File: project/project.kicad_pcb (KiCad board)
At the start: 2 copper layers, 85.5 x 86 mm, 260 parts, among them J1 FFC Connector, J2 input_1x5, J3 input_1x5, J4 input_1x5, J5 input_1x5, J6 input_1x5, J7 input_1x5, J8 input_1x5, J9 input_1x5, Q1 MMBTA44, Q10 MMBTA44, Q11 MMBTA44, Q12 MMBTA44, Q13 MMBTA44, Q14 MMBTA44, Q15 MMBTA44, Q16 MMBTA44, Q2 MMBTA44, Q3 MMBTA44, Q4 MMBTA44, Q5 MMBTA44, Q6 MMBTA44, Q7 MMBTA44, Q8 MMBTA44, Q9 MMBTA44, U1 PCA9555PW, U10 LTV-244-GB-G, U2 74HC165, U3 ISO1540, U4 GX101, U5 74HC165, U6 LTV-244-GB-G, U7 LTV-244-GB-G, U8 LTV-244-GB-G, U9 L78L05

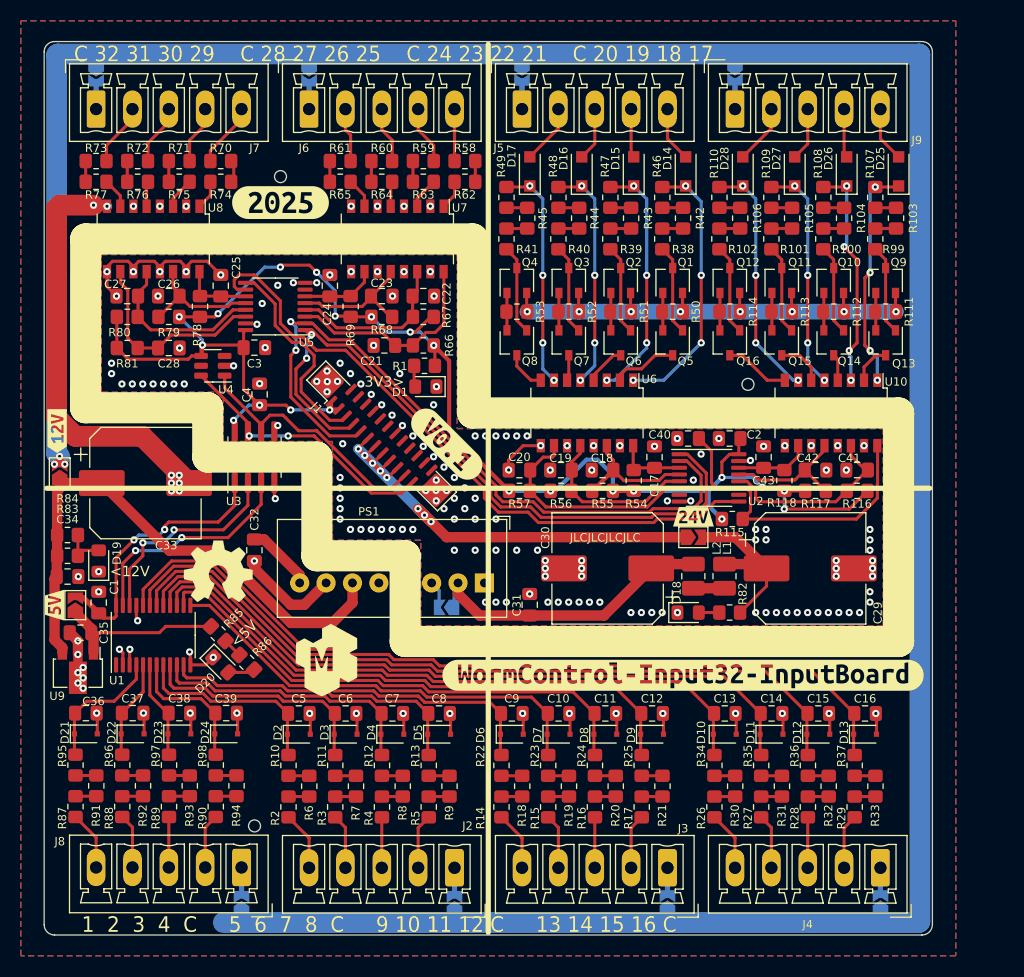
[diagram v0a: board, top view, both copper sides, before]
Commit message: refactoring everything to use selected input type
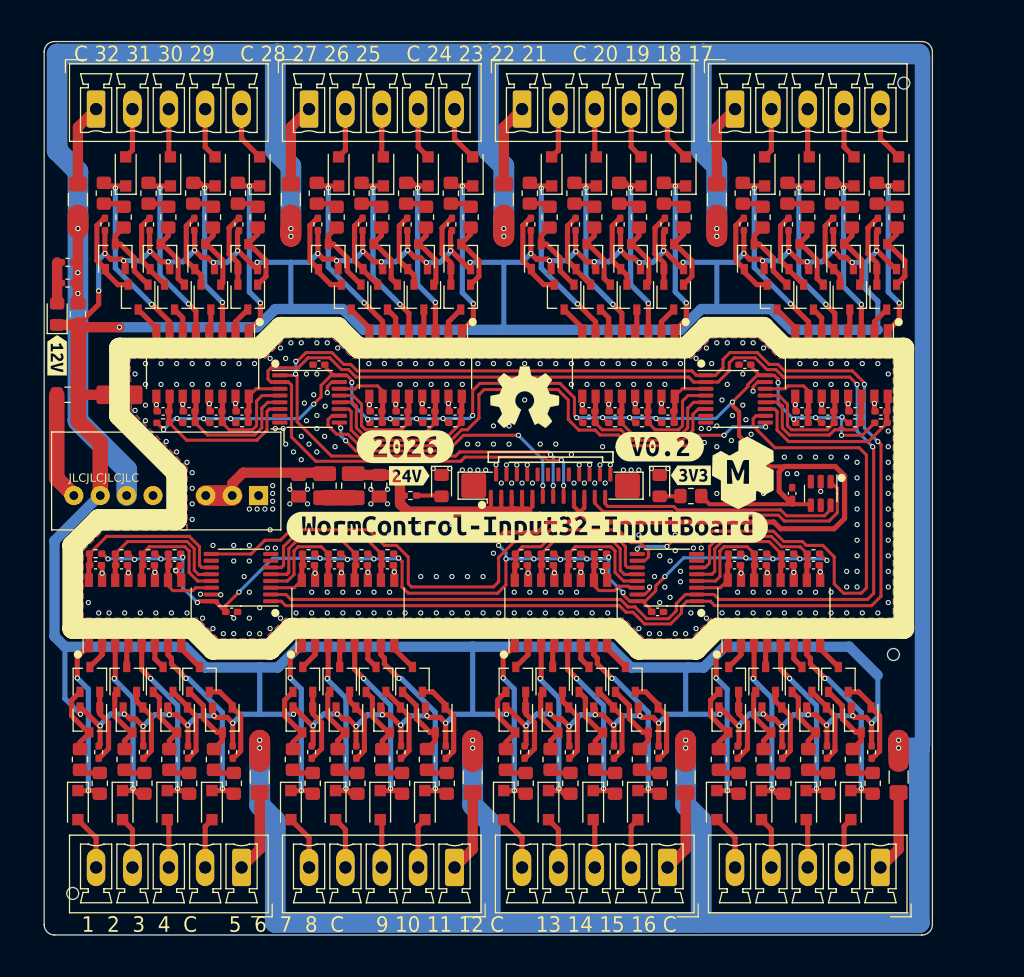
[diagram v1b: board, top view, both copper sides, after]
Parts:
- removed C1, C18, C19, C20, C21, C22, C23, C24, C25, C26, C27, C28, C34, C35, C41, C42, C43: 100n, Capacitor_SMD:C_0805_2012Metric_Pad1.18x1.45mm_HandSolder
- removed C10, C11, C12, C13, C14, C15, C16, C36, C37, C38, C39, C5, C6, C7, C8, C9: 10n, Capacitor_SMD:C_0805_2012Metric_Pad1.18x1.45mm_HandSolder
- removed C29, C30, C33: 220u/35v, Capacitor_SMD:CP_Elec_10x10.5
- removed D10, D11, D12, D13, D2, D21, D22, D23, D24, D3, D4, D5, D6, D7, D8, D9: UDZVTE-175.1B, Diode_SMD:D_SOD-323F
- removed D15, D16, D17, D26, D27, D28: SM4007PL, Diode_SMD:D_SOD-123F
- removed D20: GREEN, LED_SMD:LED_0805_2012Metric_Pad1.15x1.40mm_HandSolder
- removed J2, J3, J4, J6, J7, J8: input_1x5, Connector_Phoenix_MC:PhoenixContact_MCV_1,5_5-G-3.5_1x05_P3.50mm_Vertical
- removed JP1, JP10, JP11, JP12, JP2, JP3, JP4, JP5, JP6, JP7, JP8, JP9: SolderJumper_2_Open, Jumper:SolderJumper-2_P1.3mm_Open_TrianglePad1.0x1.5mm
- removed Q10, Q11, Q12, Q14, Q15, Q16, Q2, Q3, Q4, Q6, Q7, Q8: MMBTA44, Package_TO_SOT_SMD:SOT-23W
- removed R10, R100, R102, R104, R105, R106, R108, R109, R11, R110, R12, R13, R14, R15, R16, R17, R18, R19, R2, R20, R21, R22, R23, R24, R25, R26, R27, R28, R29, R3, R30, R31, R32, R33, R34, R35, R36, R37, R38, R39, R4, R40, R41, R43, R44, R45, R47, R48, R49, R5, R6, R7, R8, R87, R88, R89, R9, R90, R91, R92, R93, R94, R95, R96, R97, R98, R99: 150k, Resistor_SMD:R_0805_2012Metric_Pad1.20x1.40mm_HandSolder
- removed the R101 at (195.5, 67.0)
- removed R112, R113, R114, R51, R52, R53: 330R, Resistor_SMD:R_0805_2012Metric_Pad1.20x1.40mm_HandSolder
- removed R116, R117, R118, R55, R56, R57, R66, R67, R68, R69, R78, R79, R80, R81: 47k, Resistor_SMD:R_0805_2012Metric_Pad1.20x1.40mm_HandSolder
- removed R58, R59, R60, R61, R62, R63, R64, R65, R70, R71, R72, R73, R74, R75, R76, R77: 1k2, Resistor_SMD:R_0805_2012Metric_Pad1.20x1.40mm_HandSolder
- removed R85, R86: 4k7, Resistor_SMD:R_0805_2012Metric_Pad1.20x1.40mm_HandSolder
- removed U1: PCA9555PW, Package_SO:TSSOP-24_4.4x7.8mm_P0.65mm
- removed U10, U6, U7, U8: LTV-244-GB-G, Package_SO:SOP-16_4.4x10.4mm_P1.27mm
- removed U3: ISO1540, Package_SO:SOIC-8_3.9x4.9mm_P1.27mm
- removed U9: L78L05, Package_TO_SOT_SMD:SOT-89-3
- removed kibuzzard-68463028: G***, kibuzzard-68463028
- removed kibuzzard-68463097: G***, kibuzzard-68463097
- removed kibuzzard-68463581: G***, kibuzzard-68463581
- removed kibuzzard-68463930: G***, kibuzzard-68463930
- removed kibuzzard-68463AFF: G***, kibuzzard-68463AFF
- removed kibuzzard-68463C37 (x8): G***, kibuzzard-68463C37
- removed kibuzzard-68464180: G***, kibuzzard-68464180
- added C1002: 100n, Capacitor_SMD:C_0402_1005Metric_Pad0.74x0.62mm_HandSolder, F.Cu at (133.0, 98.4)
- added C1003: 100n, Capacitor_SMD:C_0402_1005Metric_Pad0.74x0.62mm_HandSolder, F.Cu at (135.6, 98.4)
- added C1004: 100n, Capacitor_SMD:C_0402_1005Metric_Pad0.74x0.62mm_HandSolder, F.Cu at (138.1, 98.4)
- added C102: 100n, Capacitor_SMD:C_0402_1005Metric_Pad0.74x0.62mm_HandSolder, F.Cu at (193.0, 79.1)
- added C105: 100n, Capacitor_SMD:C_0402_1005Metric_Pad0.74x0.62mm_HandSolder, F.Cu at (152.0, 79.1)
- added C201: 100n, Capacitor_SMD:C_0402_1005Metric_Pad0.74x0.62mm_HandSolder, F.Cu at (171.5, 98.4)
- added C202: 100n, Capacitor_SMD:C_0402_1005Metric_Pad0.74x0.62mm_HandSolder, F.Cu at (174.0, 98.4)
- added C203: 100n, Capacitor_SMD:C_0402_1005Metric_Pad0.74x0.62mm_HandSolder, F.Cu at (176.6, 98.4)
- added C204: 100n, Capacitor_SMD:C_0402_1005Metric_Pad0.74x0.62mm_HandSolder, F.Cu at (179.1, 98.4)
- added C301: 100n, Capacitor_SMD:C_0402_1005Metric_Pad0.74x0.62mm_HandSolder, F.Cu at (192.0, 98.4)
- added C302: 100n, Capacitor_SMD:C_0402_1005Metric_Pad0.74x0.62mm_HandSolder, F.Cu at (194.5, 98.4)
- added C303: 100n, Capacitor_SMD:C_0402_1005Metric_Pad0.74x0.62mm_HandSolder, F.Cu at (197.1, 98.4)
- added C304: 100n, Capacitor_SMD:C_0402_1005Metric_Pad0.74x0.62mm_HandSolder, F.Cu at (199.6, 98.4)
- added C401: 100n, Capacitor_SMD:C_0402_1005Metric_Pad0.74x0.62mm_HandSolder, F.Cu at (185.6, 83.6)
- added C402: 100n, Capacitor_SMD:C_0402_1005Metric_Pad0.74x0.62mm_HandSolder, F.Cu at (183.1, 83.6)
- added C403: 100n, Capacitor_SMD:C_0402_1005Metric_Pad0.74x0.62mm_HandSolder, F.Cu at (180.5, 83.6)
- added C404: 100n, Capacitor_SMD:C_0402_1005Metric_Pad0.74x0.62mm_HandSolder, F.Cu at (178.0, 83.6)
- added C502: 100n, Capacitor_SMD:C_0402_1005Metric_Pad0.74x0.62mm_HandSolder, F.Cu at (153.5, 98.4)
- added C503: 100n, Capacitor_SMD:C_0402_1005Metric_Pad0.74x0.62mm_HandSolder, F.Cu at (156.1, 98.4)
- added C504: 100n, Capacitor_SMD:C_0402_1005Metric_Pad0.74x0.62mm_HandSolder, F.Cu at (158.6, 98.4)
- added C601: 100n, Capacitor_SMD:C_0402_1005Metric_Pad0.74x0.62mm_HandSolder, F.Cu at (206.1, 83.6)
- added C602: 100n, Capacitor_SMD:C_0402_1005Metric_Pad0.74x0.62mm_HandSolder, F.Cu at (203.6, 83.6)
- added C603: 100n, Capacitor_SMD:C_0402_1005Metric_Pad0.74x0.62mm_HandSolder, F.Cu at (201.0, 83.6)
- added C604: 100n, Capacitor_SMD:C_0402_1005Metric_Pad0.74x0.62mm_HandSolder, F.Cu at (198.5, 83.6)
- added C701: 100n, Capacitor_SMD:C_0402_1005Metric_Pad0.74x0.62mm_HandSolder, F.Cu at (165.1, 83.6)
- added C702: 100n, Capacitor_SMD:C_0402_1005Metric_Pad0.74x0.62mm_HandSolder, F.Cu at (162.6, 83.6)
- added C703: 100n, Capacitor_SMD:C_0402_1005Metric_Pad0.74x0.62mm_HandSolder, F.Cu at (160.0, 83.6)
- added C704: 100n, Capacitor_SMD:C_0402_1005Metric_Pad0.74x0.62mm_HandSolder, F.Cu at (157.5, 83.6)
- added C801: 100n, Capacitor_SMD:C_0402_1005Metric_Pad0.74x0.62mm_HandSolder, F.Cu at (144.6, 83.6)
- added C802: 100n, Capacitor_SMD:C_0402_1005Metric_Pad0.74x0.62mm_HandSolder, F.Cu at (142.1, 83.6)
- added C803: 100n, Capacitor_SMD:C_0402_1005Metric_Pad0.74x0.62mm_HandSolder, F.Cu at (139.5, 83.6)
- added C804: 100n, Capacitor_SMD:C_0402_1005Metric_Pad0.74x0.62mm_HandSolder, F.Cu at (137.0, 83.6)
- added C901: 10u/50v, Capacitor_SMD:C_0805_2012Metric_Pad1.18x1.45mm_HandSolder, F.Cu at (157.8, 90.8)
- added C903: 1n/2KV, Capacitor_SMD:C_1206_3216Metric_Pad1.33x1.80mm_HandSolder, F.Cu at (132.8, 82.0)
- added C905: 22u/25v, Capacitor_SMD:C_0805_2012Metric_Pad1.18x1.45mm_HandSolder, F.Cu at (128.8, 74.3)
- added D1002: SM4007PL, Diode_SMD:D_SOD-123F, F.Cu at (133.1, 121.5)
- added D1003: SM4007PL, Diode_SMD:D_SOD-123F, F.Cu at (137.4, 121.5)
- added D1004: SM4007PL, Diode_SMD:D_SOD-123F, F.Cu at (141.7, 121.5)
- added D201: SM4007PL, Diode_SMD:D_SOD-123F, F.Cu at (169.8, 121.5)
- added D202: SM4007PL, Diode_SMD:D_SOD-123F, F.Cu at (174.1, 121.5)
- added D203: SM4007PL, Diode_SMD:D_SOD-123F, F.Cu at (178.4, 121.5)
- added D204: SM4007PL, Diode_SMD:D_SOD-123F, F.Cu at (182.7, 121.5)
- added D301: SM4007PL, Diode_SMD:D_SOD-123F, F.Cu at (190.3, 121.5)
- added D302: SM4007PL, Diode_SMD:D_SOD-123F, F.Cu at (194.6, 121.5)
- added D303: SM4007PL, Diode_SMD:D_SOD-123F, F.Cu at (198.9, 121.5)
- added D304: SM4007PL, Diode_SMD:D_SOD-123F, F.Cu at (203.2, 121.5)
- added D401: SM4007PL, Diode_SMD:D_SOD-123F, F.Cu at (187.3, 60.5)
- added D402: SM4007PL, Diode_SMD:D_SOD-123F, F.Cu at (183.0, 60.5)
- added D403: SM4007PL, Diode_SMD:D_SOD-123F, F.Cu at (178.7, 60.5)
- added D404: SM4007PL, Diode_SMD:D_SOD-123F, F.Cu at (174.4, 60.5)
- added D502: SM4007PL, Diode_SMD:D_SOD-123F, F.Cu at (153.6, 121.5)
- added D503: SM4007PL, Diode_SMD:D_SOD-123F, F.Cu at (157.9, 121.5)
- added D504: SM4007PL, Diode_SMD:D_SOD-123F, F.Cu at (162.2, 121.5)
- added D601: SM4007PL, Diode_SMD:D_SOD-123F, F.Cu at (207.8, 60.5)
- added D602: SM4007PL, Diode_SMD:D_SOD-123F, F.Cu at (203.5, 60.5)
- added D603: SM4007PL, Diode_SMD:D_SOD-123F, F.Cu at (199.2, 60.5)
- added D604: SM4007PL, Diode_SMD:D_SOD-123F, F.Cu at (194.9, 60.5)
- added D701: SM4007PL, Diode_SMD:D_SOD-123F, F.Cu at (166.8, 60.5)
- added D702: SM4007PL, Diode_SMD:D_SOD-123F, F.Cu at (162.5, 60.5)
- added D703: SM4007PL, Diode_SMD:D_SOD-123F, F.Cu at (158.2, 60.5)
- added D704: SM4007PL, Diode_SMD:D_SOD-123F, F.Cu at (153.9, 60.5)
- added D801: SM4007PL, Diode_SMD:D_SOD-123F, F.Cu at (146.3, 60.5)
- added D802: SM4007PL, Diode_SMD:D_SOD-123F, F.Cu at (142.0, 60.5)
- added D803: SM4007PL, Diode_SMD:D_SOD-123F, F.Cu at (137.7, 60.5)
- added D804: SM4007PL, Diode_SMD:D_SOD-123F, F.Cu at (133.4, 60.5)
- added F1001: 50mA, Fuse:Fuse_1206_3216Metric_Pad1.42x1.75mm_HandSolder, F.Cu at (146.3, 118.8)
- added F201: 50mA, Fuse:Fuse_1206_3216Metric_Pad1.42x1.75mm_HandSolder, F.Cu at (187.3, 118.8)
- added F301: 50mA, Fuse:Fuse_1206_3216Metric_Pad1.42x1.75mm_HandSolder, F.Cu at (207.8, 118.8)
- added F401: 50mA, Fuse:Fuse_1206_3216Metric_Pad1.42x1.75mm_HandSolder, F.Cu at (169.8, 63.2)
- added F501: 50mA, Fuse:Fuse_1206_3216Metric_Pad1.42x1.75mm_HandSolder, F.Cu at (166.8, 118.8)
- added F601: 50mA, Fuse:Fuse_1206_3216Metric_Pad1.42x1.75mm_HandSolder, F.Cu at (190.3, 63.2)
- added F701: 50mA, Fuse:Fuse_1206_3216Metric_Pad1.42x1.75mm_HandSolder, F.Cu at (149.3, 63.2)
- added F801: 50mA, Fuse:Fuse_1206_3216Metric_Pad1.42x1.75mm_HandSolder, F.Cu at (128.8, 63.2)
- added J201: input_1x5, Connector_Phoenix_MC:PhoenixContact_MCV_1,5_5-G-3.5_1x05_P3.50mm_Vertical, F.Cu at (185.5, 127.5)
- added J301: input_1x5, Connector_Phoenix_MC:PhoenixContact_MCV_1,5_5-G-3.5_1x05_P3.50mm_Vertical, F.Cu at (206.0, 127.5)
- added J401: input_1x5, Connector_Phoenix_MC:PhoenixContact_MCV_1,5_5-G-3.5_1x05_P3.50mm_Vertical, F.Cu at (171.5, 54.5)
- added J601: input_1x5, Connector_Phoenix_MC:PhoenixContact_MCV_1,5_5-G-3.5_1x05_P3.50mm_Vertical, F.Cu at (192.0, 54.5)
- added J701: input_1x5, Connector_Phoenix_MC:PhoenixContact_MCV_1,5_5-G-3.5_1x05_P3.50mm_Vertical, F.Cu at (151.0, 54.5)
- added J801: input_1x5, Connector_Phoenix_MC:PhoenixContact_MCV_1,5_5-G-3.5_1x05_P3.50mm_Vertical, F.Cu at (130.5, 54.5)
- added Q1002: MMBTA44, Package_TO_SOT_SMD:SOT-23W, F.Cu at (134.1, 113.3)
- added Q1003: MMBTA44, Package_TO_SOT_SMD:SOT-23W, F.Cu at (138.4, 113.3)
- added Q1004: MMBTA44, Package_TO_SOT_SMD:SOT-23W, F.Cu at (142.7, 113.3)
- added Q1006: MMBTA44, Package_TO_SOT_SMD:SOT-23W, F.Cu at (133.5, 109.4)
- added Q1007: MMBTA44, Package_TO_SOT_SMD:SOT-23W, F.Cu at (137.0, 109.4)
- added Q1008: MMBTA44, Package_TO_SOT_SMD:SOT-23W, F.Cu at (140.5, 109.4)
- added Q201: MMBTA44, Package_TO_SOT_SMD:SOT-23W, F.Cu at (170.9, 113.3)
- added Q202: MMBTA44, Package_TO_SOT_SMD:SOT-23W, F.Cu at (175.1, 113.3)
- added Q203: MMBTA44, Package_TO_SOT_SMD:SOT-23W, F.Cu at (179.4, 113.3)
- added Q204: MMBTA44, Package_TO_SOT_SMD:SOT-23W, F.Cu at (183.7, 113.3)
- added Q205: MMBTA44, Package_TO_SOT_SMD:SOT-23W, F.Cu at (170.9, 109.4)
- added Q206: MMBTA44, Package_TO_SOT_SMD:SOT-23W, F.Cu at (174.5, 109.4)
- added Q207: MMBTA44, Package_TO_SOT_SMD:SOT-23W, F.Cu at (178.0, 109.4)
- added Q208: MMBTA44, Package_TO_SOT_SMD:SOT-23W, F.Cu at (181.5, 109.4)
- added Q301: MMBTA44, Package_TO_SOT_SMD:SOT-23W, F.Cu at (191.4, 113.3)
- added Q302: MMBTA44, Package_TO_SOT_SMD:SOT-23W, F.Cu at (195.6, 113.3)
- added Q303: MMBTA44, Package_TO_SOT_SMD:SOT-23W, F.Cu at (199.9, 113.3)
- added Q304: MMBTA44, Package_TO_SOT_SMD:SOT-23W, F.Cu at (204.2, 113.3)
- added Q305: MMBTA44, Package_TO_SOT_SMD:SOT-23W, F.Cu at (191.4, 109.4)
- added Q306: MMBTA44, Package_TO_SOT_SMD:SOT-23W, F.Cu at (195.0, 109.4)
- added Q307: MMBTA44, Package_TO_SOT_SMD:SOT-23W, F.Cu at (198.5, 109.4)
- added Q308: MMBTA44, Package_TO_SOT_SMD:SOT-23W, F.Cu at (202.0, 109.4)
- added Q401: MMBTA44, Package_TO_SOT_SMD:SOT-23W, F.Cu at (186.1, 68.7)
- added Q402: MMBTA44, Package_TO_SOT_SMD:SOT-23W, F.Cu at (182.0, 68.7)
- added Q403: MMBTA44, Package_TO_SOT_SMD:SOT-23W, F.Cu at (177.7, 68.7)
- added Q404: MMBTA44, Package_TO_SOT_SMD:SOT-23W, F.Cu at (173.4, 68.7)
- added Q405: MMBTA44, Package_TO_SOT_SMD:SOT-23W, F.Cu at (186.1, 72.6)
- added Q406: MMBTA44, Package_TO_SOT_SMD:SOT-23W, F.Cu at (182.6, 72.6)
- added Q407: MMBTA44, Package_TO_SOT_SMD:SOT-23W, F.Cu at (179.1, 72.6)
- added Q408: MMBTA44, Package_TO_SOT_SMD:SOT-23W, F.Cu at (175.6, 72.6)
- added Q502: MMBTA44, Package_TO_SOT_SMD:SOT-23W, F.Cu at (154.6, 113.3)
- added Q503: MMBTA44, Package_TO_SOT_SMD:SOT-23W, F.Cu at (158.9, 113.3)
- added Q504: MMBTA44, Package_TO_SOT_SMD:SOT-23W, F.Cu at (163.2, 113.3)
- added Q506: MMBTA44, Package_TO_SOT_SMD:SOT-23W, F.Cu at (154.0, 109.4)
- added Q507: MMBTA44, Package_TO_SOT_SMD:SOT-23W, F.Cu at (157.5, 109.4)
- added Q508: MMBTA44, Package_TO_SOT_SMD:SOT-23W, F.Cu at (161.0, 109.4)
- added Q601: MMBTA44, Package_TO_SOT_SMD:SOT-23W, F.Cu at (206.6, 68.7)
- added Q602: MMBTA44, Package_TO_SOT_SMD:SOT-23W, F.Cu at (202.5, 68.7)
- added Q603: MMBTA44, Package_TO_SOT_SMD:SOT-23W, F.Cu at (198.2, 68.7)
- added Q604: MMBTA44, Package_TO_SOT_SMD:SOT-23W, F.Cu at (193.9, 68.7)
- added Q605: MMBTA44, Package_TO_SOT_SMD:SOT-23W, F.Cu at (206.6, 72.6)
- added Q606: MMBTA44, Package_TO_SOT_SMD:SOT-23W, F.Cu at (203.1, 72.6)
- added Q607: MMBTA44, Package_TO_SOT_SMD:SOT-23W, F.Cu at (199.6, 72.6)
- added Q608: MMBTA44, Package_TO_SOT_SMD:SOT-23W, F.Cu at (196.1, 72.6)
- added Q701: MMBTA44, Package_TO_SOT_SMD:SOT-23W, F.Cu at (165.6, 68.7)
- added Q702: MMBTA44, Package_TO_SOT_SMD:SOT-23W, F.Cu at (161.5, 68.7)
- added Q703: MMBTA44, Package_TO_SOT_SMD:SOT-23W, F.Cu at (157.2, 68.7)
- added Q704: MMBTA44, Package_TO_SOT_SMD:SOT-23W, F.Cu at (152.9, 68.7)
- added Q705: MMBTA44, Package_TO_SOT_SMD:SOT-23W, F.Cu at (165.6, 72.6)
- added Q706: MMBTA44, Package_TO_SOT_SMD:SOT-23W, F.Cu at (162.1, 72.6)
- added Q707: MMBTA44, Package_TO_SOT_SMD:SOT-23W, F.Cu at (158.6, 72.6)
- added Q708: MMBTA44, Package_TO_SOT_SMD:SOT-23W, F.Cu at (155.1, 72.6)
- added Q801: MMBTA44, Package_TO_SOT_SMD:SOT-23W, F.Cu at (145.1, 68.7)
- added Q802: MMBTA44, Package_TO_SOT_SMD:SOT-23W, F.Cu at (141.0, 68.7)
- added Q803: MMBTA44, Package_TO_SOT_SMD:SOT-23W, F.Cu at (136.7, 68.7)
- added Q804: MMBTA44, Package_TO_SOT_SMD:SOT-23W, F.Cu at (132.4, 68.7)
- added Q805: MMBTA44, Package_TO_SOT_SMD:SOT-23W, F.Cu at (145.1, 72.6)
- added Q806: MMBTA44, Package_TO_SOT_SMD:SOT-23W, F.Cu at (141.6, 72.6)
- added Q807: MMBTA44, Package_TO_SOT_SMD:SOT-23W, F.Cu at (138.1, 72.6)
- added Q808: MMBTA44, Package_TO_SOT_SMD:SOT-23W, F.Cu at (134.6, 72.6)
- added R1002: 220k, Resistor_SMD:R_0805_2012Metric_Pad1.20x1.40mm_HandSolder, F.Cu at (133.3, 117.1)
- added R1003: 220k, Resistor_SMD:R_0805_2012Metric_Pad1.20x1.40mm_HandSolder, F.Cu at (137.6, 117.1)
- added R1004: 220k, Resistor_SMD:R_0805_2012Metric_Pad1.20x1.40mm_HandSolder, F.Cu at (141.9, 117.1)
- added R1006: 220k, Resistor_SMD:R_0805_2012Metric_Pad1.20x1.40mm_HandSolder, F.Cu at (135.2, 119.4)
- added R1007: 220k, Resistor_SMD:R_0805_2012Metric_Pad1.20x1.40mm_HandSolder, F.Cu at (139.5, 119.4)
- added R1008: 220k, Resistor_SMD:R_0805_2012Metric_Pad1.20x1.40mm_HandSolder, F.Cu at (143.8, 119.4)
- added R1010: 330R, Resistor_SMD:R_0402_1005Metric_Pad0.72x0.64mm_HandSolder, F.Cu at (135.1, 116.4)
- added R1011: 330R, Resistor_SMD:R_0402_1005Metric_Pad0.72x0.64mm_HandSolder, F.Cu at (139.4, 116.4)
- added R1012: 330R, Resistor_SMD:R_0402_1005Metric_Pad0.72x0.64mm_HandSolder, F.Cu at (143.7, 116.4)
- added R1014: 47k, Resistor_SMD:R_0402_1005Metric_Pad0.72x0.64mm_HandSolder, F.Cu at (133.0, 97.3)
- added R1015: 47k, Resistor_SMD:R_0402_1005Metric_Pad0.72x0.64mm_HandSolder, F.Cu at (135.6, 97.3)
- added R1016: 47k, Resistor_SMD:R_0402_1005Metric_Pad0.72x0.64mm_HandSolder, F.Cu at (138.1, 97.3)
- added R201: 220k, Resistor_SMD:R_0805_2012Metric_Pad1.20x1.40mm_HandSolder, F.Cu at (170.0, 117.1)
- added R202: 220k, Resistor_SMD:R_0805_2012Metric_Pad1.20x1.40mm_HandSolder, F.Cu at (174.3, 117.1)
- added R203: 220k, Resistor_SMD:R_0805_2012Metric_Pad1.20x1.40mm_HandSolder, F.Cu at (178.6, 117.1)
- added R204: 220k, Resistor_SMD:R_0805_2012Metric_Pad1.20x1.40mm_HandSolder, F.Cu at (182.9, 117.1)
- added R205: 220k, Resistor_SMD:R_0805_2012Metric_Pad1.20x1.40mm_HandSolder, F.Cu at (171.9, 119.4)
- added R206: 220k, Resistor_SMD:R_0805_2012Metric_Pad1.20x1.40mm_HandSolder, F.Cu at (176.2, 119.4)
- added R207: 220k, Resistor_SMD:R_0805_2012Metric_Pad1.20x1.40mm_HandSolder, F.Cu at (180.5, 119.4)
- added R208: 220k, Resistor_SMD:R_0805_2012Metric_Pad1.20x1.40mm_HandSolder, F.Cu at (184.8, 119.4)
- added R209: 330R, Resistor_SMD:R_0402_1005Metric_Pad0.72x0.64mm_HandSolder, F.Cu at (171.8, 116.4)
- added R210: 330R, Resistor_SMD:R_0402_1005Metric_Pad0.72x0.64mm_HandSolder, F.Cu at (176.1, 116.4)
- added R211: 330R, Resistor_SMD:R_0402_1005Metric_Pad0.72x0.64mm_HandSolder, F.Cu at (180.4, 116.4)
- added R212: 330R, Resistor_SMD:R_0402_1005Metric_Pad0.72x0.64mm_HandSolder, F.Cu at (184.7, 116.4)
- added R213: 47k, Resistor_SMD:R_0402_1005Metric_Pad0.72x0.64mm_HandSolder, F.Cu at (171.5, 97.3)
- added R214: 47k, Resistor_SMD:R_0402_1005Metric_Pad0.72x0.64mm_HandSolder, F.Cu at (174.0, 97.3)
- added R215: 47k, Resistor_SMD:R_0402_1005Metric_Pad0.72x0.64mm_HandSolder, F.Cu at (176.6, 97.3)
- added R216: 47k, Resistor_SMD:R_0402_1005Metric_Pad0.72x0.64mm_HandSolder, F.Cu at (179.1, 97.3)
- added R301: 220k, Resistor_SMD:R_0805_2012Metric_Pad1.20x1.40mm_HandSolder, F.Cu at (190.5, 117.1)
- added R302: 220k, Resistor_SMD:R_0805_2012Metric_Pad1.20x1.40mm_HandSolder, F.Cu at (194.8, 117.1)
- added R303: 220k, Resistor_SMD:R_0805_2012Metric_Pad1.20x1.40mm_HandSolder, F.Cu at (199.1, 117.1)
- added R304: 220k, Resistor_SMD:R_0805_2012Metric_Pad1.20x1.40mm_HandSolder, F.Cu at (203.4, 117.1)
- added R305: 220k, Resistor_SMD:R_0805_2012Metric_Pad1.20x1.40mm_HandSolder, F.Cu at (192.4, 119.4)
- added R306: 220k, Resistor_SMD:R_0805_2012Metric_Pad1.20x1.40mm_HandSolder, F.Cu at (196.7, 119.4)
- added R307: 220k, Resistor_SMD:R_0805_2012Metric_Pad1.20x1.40mm_HandSolder, F.Cu at (201.0, 119.4)
- added R308: 220k, Resistor_SMD:R_0805_2012Metric_Pad1.20x1.40mm_HandSolder, F.Cu at (205.3, 119.4)
- added R309: 330R, Resistor_SMD:R_0402_1005Metric_Pad0.72x0.64mm_HandSolder, F.Cu at (192.3, 116.4)
- added R310: 330R, Resistor_SMD:R_0402_1005Metric_Pad0.72x0.64mm_HandSolder, F.Cu at (196.6, 116.4)
- added R311: 330R, Resistor_SMD:R_0402_1005Metric_Pad0.72x0.64mm_HandSolder, F.Cu at (200.9, 116.4)
- added R312: 330R, Resistor_SMD:R_0402_1005Metric_Pad0.72x0.64mm_HandSolder, F.Cu at (205.2, 116.4)
- added R313: 47k, Resistor_SMD:R_0402_1005Metric_Pad0.72x0.64mm_HandSolder, F.Cu at (192.0, 97.3)
- added R314: 47k, Resistor_SMD:R_0402_1005Metric_Pad0.72x0.64mm_HandSolder, F.Cu at (194.5, 97.3)
- added R315: 47k, Resistor_SMD:R_0402_1005Metric_Pad0.72x0.64mm_HandSolder, F.Cu at (197.1, 97.3)
- added R316: 47k, Resistor_SMD:R_0402_1005Metric_Pad0.72x0.64mm_HandSolder, F.Cu at (199.6, 97.3)
- added R401: 220k, Resistor_SMD:R_0805_2012Metric_Pad1.20x1.40mm_HandSolder, F.Cu at (187.1, 64.9)
- added R402: 220k, Resistor_SMD:R_0805_2012Metric_Pad1.20x1.40mm_HandSolder, F.Cu at (182.8, 64.9)
- added R403: 220k, Resistor_SMD:R_0805_2012Metric_Pad1.20x1.40mm_HandSolder, F.Cu at (178.5, 64.9)
- added R404: 220k, Resistor_SMD:R_0805_2012Metric_Pad1.20x1.40mm_HandSolder, F.Cu at (174.2, 64.9)
- added R405: 220k, Resistor_SMD:R_0805_2012Metric_Pad1.20x1.40mm_HandSolder, F.Cu at (185.2, 62.6)
- added R406: 220k, Resistor_SMD:R_0805_2012Metric_Pad1.20x1.40mm_HandSolder, F.Cu at (180.9, 62.6)
- added R407: 220k, Resistor_SMD:R_0805_2012Metric_Pad1.20x1.40mm_HandSolder, F.Cu at (176.6, 62.6)
- added R408: 220k, Resistor_SMD:R_0805_2012Metric_Pad1.20x1.40mm_HandSolder, F.Cu at (172.3, 62.6)
- added R409: 330R, Resistor_SMD:R_0402_1005Metric_Pad0.72x0.64mm_HandSolder, F.Cu at (185.3, 65.6)
- added R410: 330R, Resistor_SMD:R_0402_1005Metric_Pad0.72x0.64mm_HandSolder, F.Cu at (181.0, 65.6)
- added R411: 330R, Resistor_SMD:R_0402_1005Metric_Pad0.72x0.64mm_HandSolder, F.Cu at (176.7, 65.6)
- added R412: 330R, Resistor_SMD:R_0402_1005Metric_Pad0.72x0.64mm_HandSolder, F.Cu at (172.4, 65.6)
- added R413: 47k, Resistor_SMD:R_0402_1005Metric_Pad0.72x0.64mm_HandSolder, F.Cu at (185.6, 84.7)
- added R414: 47k, Resistor_SMD:R_0402_1005Metric_Pad0.72x0.64mm_HandSolder, F.Cu at (183.1, 84.7)
- added R415: 47k, Resistor_SMD:R_0402_1005Metric_Pad0.72x0.64mm_HandSolder, F.Cu at (180.5, 84.7)
- added R416: 47k, Resistor_SMD:R_0402_1005Metric_Pad0.72x0.64mm_HandSolder, F.Cu at (178.0, 84.7)
- added R502: 220k, Resistor_SMD:R_0805_2012Metric_Pad1.20x1.40mm_HandSolder, F.Cu at (153.8, 117.1)
- added R503: 220k, Resistor_SMD:R_0805_2012Metric_Pad1.20x1.40mm_HandSolder, F.Cu at (158.1, 117.1)
- added R504: 220k, Resistor_SMD:R_0805_2012Metric_Pad1.20x1.40mm_HandSolder, F.Cu at (162.4, 117.1)
- added R506: 220k, Resistor_SMD:R_0805_2012Metric_Pad1.20x1.40mm_HandSolder, F.Cu at (155.7, 119.4)
- added R507: 220k, Resistor_SMD:R_0805_2012Metric_Pad1.20x1.40mm_HandSolder, F.Cu at (160.0, 119.4)
- added R508: 220k, Resistor_SMD:R_0805_2012Metric_Pad1.20x1.40mm_HandSolder, F.Cu at (164.3, 119.4)
- added R510: 330R, Resistor_SMD:R_0402_1005Metric_Pad0.72x0.64mm_HandSolder, F.Cu at (155.6, 116.4)
- added R511: 330R, Resistor_SMD:R_0402_1005Metric_Pad0.72x0.64mm_HandSolder, F.Cu at (159.9, 116.4)
- added R512: 330R, Resistor_SMD:R_0402_1005Metric_Pad0.72x0.64mm_HandSolder, F.Cu at (164.2, 116.4)
- added R514: 47k, Resistor_SMD:R_0402_1005Metric_Pad0.72x0.64mm_HandSolder, F.Cu at (153.5, 97.3)
- added R515: 47k, Resistor_SMD:R_0402_1005Metric_Pad0.72x0.64mm_HandSolder, F.Cu at (156.1, 97.3)
- added R516: 47k, Resistor_SMD:R_0402_1005Metric_Pad0.72x0.64mm_HandSolder, F.Cu at (158.6, 97.3)
- added R601: 220k, Resistor_SMD:R_0805_2012Metric_Pad1.20x1.40mm_HandSolder, F.Cu at (207.6, 64.9)
- added R602: 220k, Resistor_SMD:R_0805_2012Metric_Pad1.20x1.40mm_HandSolder, F.Cu at (203.3, 64.9)
- added R603: 220k, Resistor_SMD:R_0805_2012Metric_Pad1.20x1.40mm_HandSolder, F.Cu at (199.0, 64.9)
- added R604: 220k, Resistor_SMD:R_0805_2012Metric_Pad1.20x1.40mm_HandSolder, F.Cu at (194.7, 64.9)
- added R605: 220k, Resistor_SMD:R_0805_2012Metric_Pad1.20x1.40mm_HandSolder, F.Cu at (205.7, 62.6)
- added R606: 220k, Resistor_SMD:R_0805_2012Metric_Pad1.20x1.40mm_HandSolder, F.Cu at (201.4, 62.6)
- added R607: 220k, Resistor_SMD:R_0805_2012Metric_Pad1.20x1.40mm_HandSolder, F.Cu at (197.1, 62.6)
- added R608: 220k, Resistor_SMD:R_0805_2012Metric_Pad1.20x1.40mm_HandSolder, F.Cu at (192.8, 62.6)
- added R609: 330R, Resistor_SMD:R_0402_1005Metric_Pad0.72x0.64mm_HandSolder, F.Cu at (205.8, 65.6)
- added R610: 330R, Resistor_SMD:R_0402_1005Metric_Pad0.72x0.64mm_HandSolder, F.Cu at (201.5, 65.6)
- added R611: 330R, Resistor_SMD:R_0402_1005Metric_Pad0.72x0.64mm_HandSolder, F.Cu at (197.2, 65.6)
- added R612: 330R, Resistor_SMD:R_0402_1005Metric_Pad0.72x0.64mm_HandSolder, F.Cu at (192.9, 65.6)
- added R613: 47k, Resistor_SMD:R_0402_1005Metric_Pad0.72x0.64mm_HandSolder, F.Cu at (206.1, 84.7)
- added R614: 47k, Resistor_SMD:R_0402_1005Metric_Pad0.72x0.64mm_HandSolder, F.Cu at (203.6, 84.7)
- added R615: 47k, Resistor_SMD:R_0402_1005Metric_Pad0.72x0.64mm_HandSolder, F.Cu at (201.0, 84.7)
- added R616: 47k, Resistor_SMD:R_0402_1005Metric_Pad0.72x0.64mm_HandSolder, F.Cu at (198.5, 84.7)
- added R701: 220k, Resistor_SMD:R_0805_2012Metric_Pad1.20x1.40mm_HandSolder, F.Cu at (166.6, 64.9)
- added R702: 220k, Resistor_SMD:R_0805_2012Metric_Pad1.20x1.40mm_HandSolder, F.Cu at (162.3, 64.9)
- added R703: 220k, Resistor_SMD:R_0805_2012Metric_Pad1.20x1.40mm_HandSolder, F.Cu at (158.0, 64.9)
- added R704: 220k, Resistor_SMD:R_0805_2012Metric_Pad1.20x1.40mm_HandSolder, F.Cu at (153.7, 64.9)
- added R705: 220k, Resistor_SMD:R_0805_2012Metric_Pad1.20x1.40mm_HandSolder, F.Cu at (164.7, 62.6)
- added R706: 220k, Resistor_SMD:R_0805_2012Metric_Pad1.20x1.40mm_HandSolder, F.Cu at (160.4, 62.6)
- added R707: 220k, Resistor_SMD:R_0805_2012Metric_Pad1.20x1.40mm_HandSolder, F.Cu at (156.1, 62.6)
- added R708: 220k, Resistor_SMD:R_0805_2012Metric_Pad1.20x1.40mm_HandSolder, F.Cu at (151.8, 62.6)
- added R709: 330R, Resistor_SMD:R_0402_1005Metric_Pad0.72x0.64mm_HandSolder, F.Cu at (164.8, 65.6)
- added R710: 330R, Resistor_SMD:R_0402_1005Metric_Pad0.72x0.64mm_HandSolder, F.Cu at (160.5, 65.6)
- added R711: 330R, Resistor_SMD:R_0402_1005Metric_Pad0.72x0.64mm_HandSolder, F.Cu at (156.2, 65.6)
- added R712: 330R, Resistor_SMD:R_0402_1005Metric_Pad0.72x0.64mm_HandSolder, F.Cu at (151.9, 65.6)
- added R713: 47k, Resistor_SMD:R_0402_1005Metric_Pad0.72x0.64mm_HandSolder, F.Cu at (165.1, 84.7)
- added R714: 47k, Resistor_SMD:R_0402_1005Metric_Pad0.72x0.64mm_HandSolder, F.Cu at (162.6, 84.7)
- added R715: 47k, Resistor_SMD:R_0402_1005Metric_Pad0.72x0.64mm_HandSolder, F.Cu at (160.0, 84.7)
- added R716: 47k, Resistor_SMD:R_0402_1005Metric_Pad0.72x0.64mm_HandSolder, F.Cu at (157.5, 84.7)
- added R801: 220k, Resistor_SMD:R_0805_2012Metric_Pad1.20x1.40mm_HandSolder, F.Cu at (146.1, 64.9)
- added R802: 220k, Resistor_SMD:R_0805_2012Metric_Pad1.20x1.40mm_HandSolder, F.Cu at (141.8, 64.9)
- added R803: 220k, Resistor_SMD:R_0805_2012Metric_Pad1.20x1.40mm_HandSolder, F.Cu at (137.5, 64.9)
- added R804: 220k, Resistor_SMD:R_0805_2012Metric_Pad1.20x1.40mm_HandSolder, F.Cu at (133.2, 64.9)
- added R805: 220k, Resistor_SMD:R_0805_2012Metric_Pad1.20x1.40mm_HandSolder, F.Cu at (144.2, 62.6)
- added R806: 220k, Resistor_SMD:R_0805_2012Metric_Pad1.20x1.40mm_HandSolder, F.Cu at (139.9, 62.6)
- added R807: 220k, Resistor_SMD:R_0805_2012Metric_Pad1.20x1.40mm_HandSolder, F.Cu at (135.6, 62.6)
- added R808: 220k, Resistor_SMD:R_0805_2012Metric_Pad1.20x1.40mm_HandSolder, F.Cu at (131.3, 62.6)
- added R809: 330R, Resistor_SMD:R_0402_1005Metric_Pad0.72x0.64mm_HandSolder, F.Cu at (144.3, 65.6)
- added R810: 330R, Resistor_SMD:R_0402_1005Metric_Pad0.72x0.64mm_HandSolder, F.Cu at (140.0, 65.6)
- added R811: 330R, Resistor_SMD:R_0402_1005Metric_Pad0.72x0.64mm_HandSolder, F.Cu at (135.7, 65.6)
- added R812: 330R, Resistor_SMD:R_0402_1005Metric_Pad0.72x0.64mm_HandSolder, F.Cu at (131.4, 65.6)
- added R813: 47k, Resistor_SMD:R_0402_1005Metric_Pad0.72x0.64mm_HandSolder, F.Cu at (144.6, 84.7)
- added R814: 47k, Resistor_SMD:R_0402_1005Metric_Pad0.72x0.64mm_HandSolder, F.Cu at (142.1, 84.7)
- added R815: 47k, Resistor_SMD:R_0402_1005Metric_Pad0.72x0.64mm_HandSolder, F.Cu at (139.5, 84.7)
- added R816: 47k, Resistor_SMD:R_0402_1005Metric_Pad0.72x0.64mm_HandSolder, F.Cu at (137.0, 84.7)
- added U1001: LTV-244-GB-G, Package_SO:SOP-16_4.4x10.4mm_P1.27mm, F.Cu at (134.3, 103.0)
- added U102: 74HC165, Package_SO:TSSOP-16_4.4x5mm_P0.65mm, F.Cu at (192.1, 82.4)
- added U105: 74HC165, Package_SO:TSSOP-16_4.4x5mm_P0.65mm, F.Cu at (151.1, 82.4)
- added U201: LTV-244-GB-G, Package_SO:SOP-16_4.4x10.4mm_P1.27mm, F.Cu at (175.3, 103.0)
- added U301: LTV-244-GB-G, Package_SO:SOP-16_4.4x10.4mm_P1.27mm, F.Cu at (195.8, 103.0)
- added U401: LTV-244-GB-G, Package_SO:SOP-16_4.4x10.4mm_P1.27mm, F.Cu at (181.8, 79.0)
- added U501: LTV-244-GB-G, Package_SO:SOP-16_4.4x10.4mm_P1.27mm, F.Cu at (154.8, 103.0)
- added U601: LTV-244-GB-G, Package_SO:SOP-16_4.4x10.4mm_P1.27mm, F.Cu at (202.3, 79.0)
- added U701: LTV-244-GB-G, Package_SO:SOP-16_4.4x10.4mm_P1.27mm, F.Cu at (161.3, 79.0)
- added U801: LTV-244-GB-G, Package_SO:SOP-16_4.4x10.4mm_P1.27mm, F.Cu at (140.8, 79.0)
- added kibuzzard-69735EB9: G***, kibuzzard-69735EB9, F.Cu at (184.8, 87.0)
- added kibuzzard-69735EC0: G***, kibuzzard-69735EC0, F.Cu at (160.3, 87.0)
- added kibuzzard-69799C4A: G***, kibuzzard-69799C4A, F.Cu at (160.7, 89.8)
- added kibuzzard-69799C58: G***, kibuzzard-69799C58, F.Cu at (126.8, 78.2)
- added kibuzzard-69799C9D: G***, kibuzzard-69799C9D, F.Cu at (187.8, 89.8)
- C1001: renamed from C40; footprint Capacitor_SMD:C_0805_2012Metric_Pad1.18x1.45mm_HandSolder -> Capacitor_SMD:C_0402_1005Metric_Pad0.74x0.62mm_HandSolder
- C101: renamed from C2; footprint Capacitor_SMD:C_0805_2012Metric_Pad1.18x1.45mm_HandSolder -> Capacitor_SMD:C_0402_1005Metric_Pad0.74x0.62mm_HandSolder
- C103: renamed from C4; footprint Capacitor_SMD:C_0805_2012Metric_Pad1.18x1.45mm_HandSolder -> Capacitor_SMD:C_0402_1005Metric_Pad0.74x0.62mm_HandSolder
- C104: renamed from C3; footprint Capacitor_SMD:C_0805_2012Metric_Pad1.18x1.45mm_HandSolder -> Capacitor_SMD:C_0402_1005Metric_Pad0.74x0.62mm_HandSolder
- C501: renamed from C17; footprint Capacitor_SMD:C_0805_2012Metric_Pad1.18x1.45mm_HandSolder -> Capacitor_SMD:C_0402_1005Metric_Pad0.74x0.62mm_HandSolder
- R1001: renamed from R103; value 150k -> 220k
- R1005: renamed from R107; value 150k -> 220k
- R1009: renamed from R111; footprint Resistor_SMD:R_0805_2012Metric_Pad1.20x1.40mm_HandSolder -> Resistor_SMD:R_0402_1005Metric_Pad0.72x0.64mm_HandSolder
- R1013: renamed from R115; footprint Resistor_SMD:R_0805_2012Metric_Pad1.20x1.40mm_HandSolder -> Resistor_SMD:R_0402_1005Metric_Pad0.72x0.64mm_HandSolder
- R501: renamed from R42; value 150k -> 220k
- R505: renamed from R46; value 150k -> 220k
- R509: renamed from R50; footprint Resistor_SMD:R_0805_2012Metric_Pad1.20x1.40mm_HandSolder -> Resistor_SMD:R_0402_1005Metric_Pad0.72x0.64mm_HandSolder
- R513: renamed from R54; footprint Resistor_SMD:R_0805_2012Metric_Pad1.20x1.40mm_HandSolder -> Resistor_SMD:R_0402_1005Metric_Pad0.72x0.64mm_HandSolder
- R901: renamed from R82; footprint Resistor_SMD:R_0805_2012Metric_Pad1.20x1.40mm_HandSolder -> Resistor_SMD:R_0402_1005Metric_Pad0.72x0.64mm_HandSolder
- R902: renamed from R83; footprint Resistor_SMD:R_0805_2012Metric_Pad1.20x1.40mm_HandSolder -> Resistor_SMD:R_0402_1005Metric_Pad0.72x0.64mm_HandSolder
- R903: renamed from R84; footprint Resistor_SMD:R_0805_2012Metric_Pad1.20x1.40mm_HandSolder -> Resistor_SMD:R_0402_1005Metric_Pad0.72x0.64mm_HandSolder
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- renumbered C31 to C902, C32 to C904, D25 to D1001, D1 to D101, D14 to D501, D18 to D901, D19 to D902, G1 to G101, G2 to G102, J9 to J1001, J1 to J101, J5 to J501, L1 to L901, L2 to L902, PS1 to PS901, Q9 to Q1001, Q13 to Q1005, Q1 to Q501, Q5 to Q505, R1 to R101, U2 to U101, U4 to U103, U5 to U104
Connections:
- net /_ser_link_1 renamed /_ser_link_3
- net /input2-1/O1 renamed /input1/O1
- net /input2-2/O1 renamed /input2/O1
- net Net-(D14-Pad1) renamed /input2/OP11
- net Net-(D25-Pad1) renamed /input1/OP11
- net Net-(Q1-Pad1) renamed /input2/B12
- net Net-(Q9-Pad1) renamed /input1/B12
- C902 pad 1: Net-(C30-Pad1) -> Net-(C902-Pad1)
- J1001 pad 1: /input2-1/12V -> Net-(F1001-Pad1)
- J101 pad 1: +3V3 -> +24V
- J101 pad 11: +24V -> SER_DATA
- J101 pad 13: +24V -> SER_PL
- J101 pad 15: +24V -> SER_CLK
- J101 pad 17: +24V -> +3V3
- J101 pad 19: +24V -> +3V3
- J101 pad 3: +3V3 -> +24V
- J101 pad 5: SER_DATA -> +24V
- J101 pad 7: SER_PL -> +24V
- J101 pad 9: SER_CLK -> +24V
- J501 pad 1: /input2-2/12V -> Net-(F501-Pad1)
- L901 pad 1: /power/24V -> +24V
- L902 pad 2: Net-(C30-Pad1) -> Net-(C902-Pad1)
- PS901 pad 2: Net-(C30-Pad1) -> Net-(C902-Pad1)
- PS901 pad 3: Net-(JP12-Pad2) -> Net-(C902-Pad1)
- PS901 pad 6: /power/12V -> +12P
- Q1001 pad 3: Net-(Q9-Pad3) -> /input1/B11
- Q1005 pad 1: Net-(Q9-Pad3) -> /input1/B11
- Q1005 pad 3: Net-(Q13-Pad3) -> /input1/OP12
- Q501 pad 3: Net-(Q1-Pad3) -> /input2/B11
- Q505 pad 1: Net-(Q1-Pad3) -> /input2/B11
- Q505 pad 3: Net-(Q5-Pad3) -> /input2/OP12
- R1001 pad 2: Net-(R103-Pad2) -> /input1/B11
- R501 pad 2: Net-(R38-Pad1) -> /input2/B11
- R901 pad 2: /power/24V -> +24V
- R902 pad 1: /power/12V -> +12P
- R903 pad 1: /power/12V -> +12P
- U101 pad 12: /input2-1/O2 -> /input1/O2
- U101 pad 13: /input2-1/O3 -> /input1/O3
- U101 pad 14: /input2-1/O4 -> /input1/O4
- U101 pad 4: /input2-2/O2 -> /input2/O2
- U101 pad 5: /input2-2/O3 -> /input2/O3
- U101 pad 6: /input2-2/O4 -> /input2/O4
- U104 pad 11: /input3-1/O1 -> /input3/O1
- U104 pad 12: /input3-1/O2 -> /input3/O2
- U104 pad 13: /input3-1/O3 -> /input3/O3
- U104 pad 14: /input3-1/O4 -> /input3/O4
- U104 pad 3: /input3-2/O1 -> /input4/O1
- U104 pad 4: /input3-2/O2 -> /input4/O2
- U104 pad 5: /input3-2/O3 -> /input4/O3
- U104 pad 6: /input3-2/O4 -> /input4/O4
- U104 pad 9: SER_DATA -> /_ser_link_2
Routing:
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- removed copper zone on B.Cu, net GNDPWR
- removed copper zone on F.Cu, net GNDPWR
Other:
- board text removed: "3V3>"
- board text removed: "<12V"
- board text removed: "<5V"

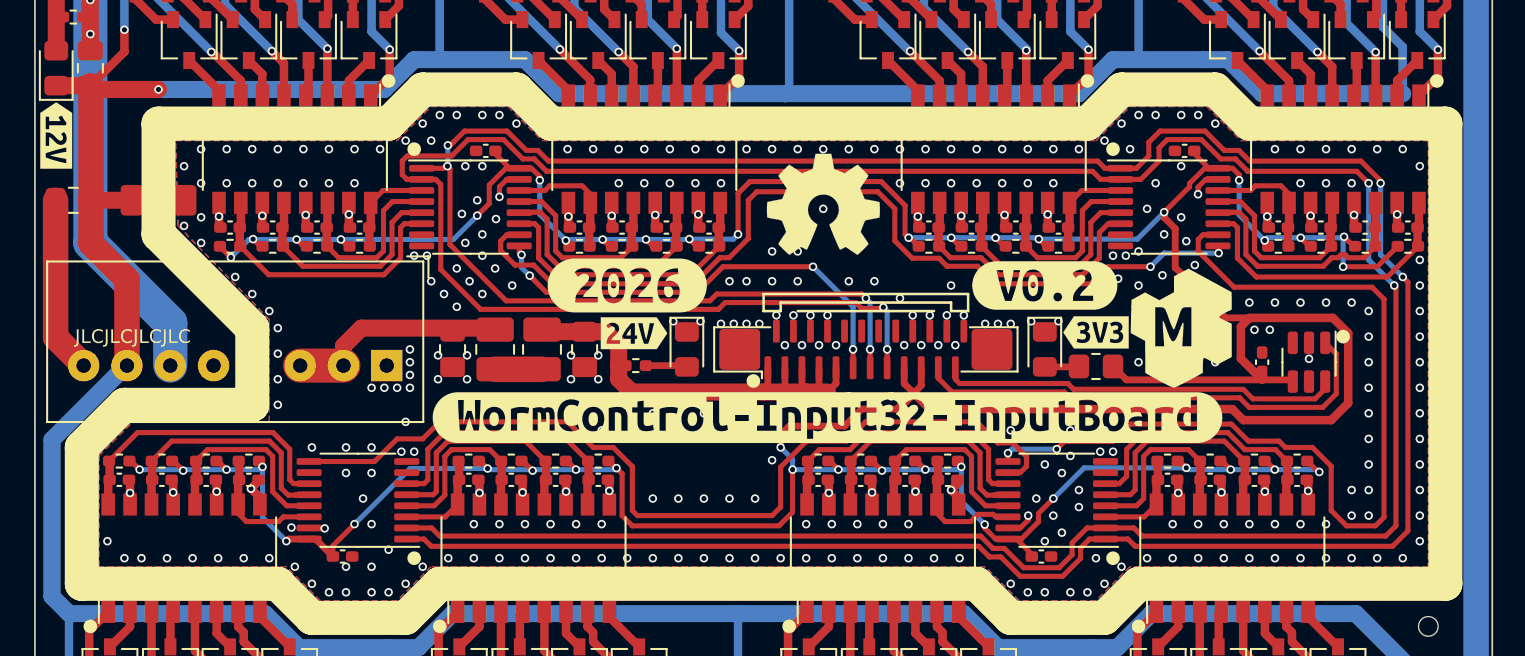
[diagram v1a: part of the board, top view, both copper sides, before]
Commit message: moving ffc connector to align with other boards
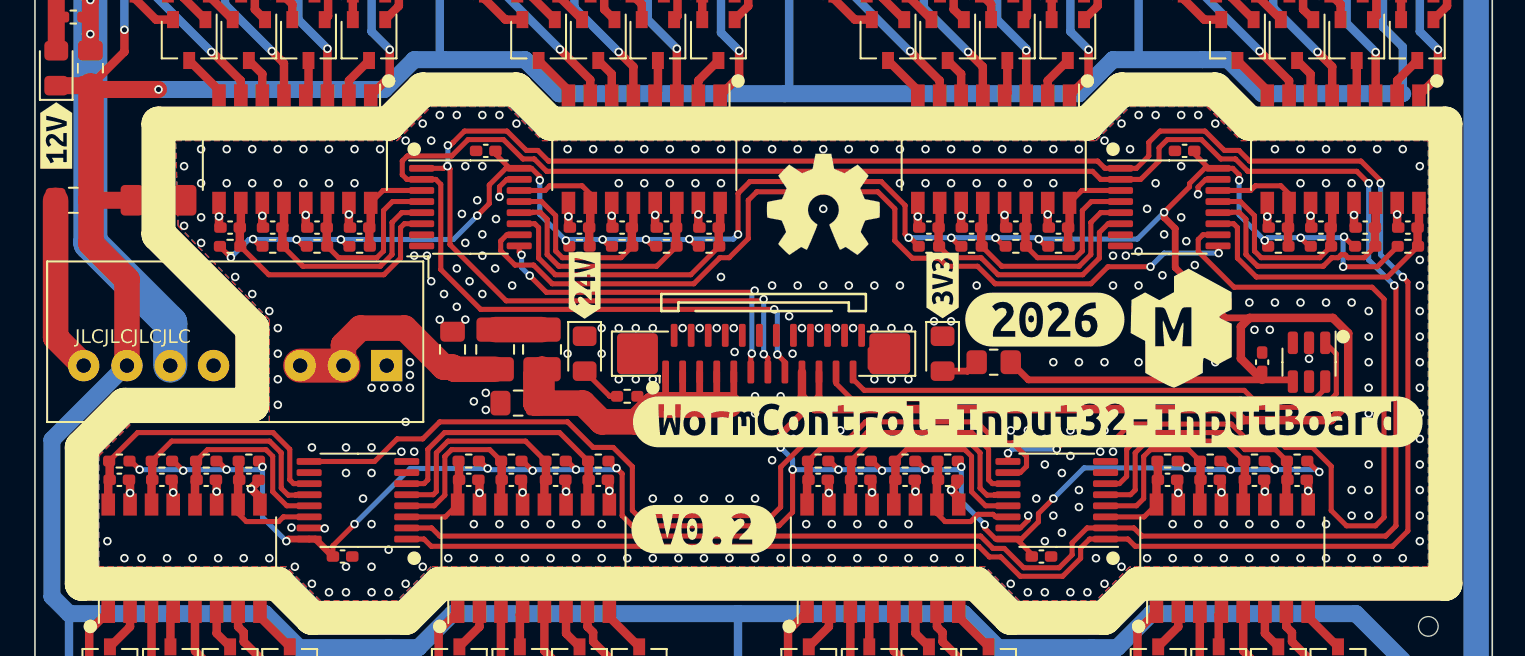
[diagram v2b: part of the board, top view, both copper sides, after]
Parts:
- removed kibuzzard-69799C4A: G***, kibuzzard-69799C4A
- removed kibuzzard-69799C58: G***, kibuzzard-69799C58
- added kibuzzard-698DC759: G***, kibuzzard-698DC759, F.Cu at (126.8, 78.2)
- added kibuzzard-698DC8DA: G***, kibuzzard-698DC8DA, F.Cu at (157.8, 87.0)
- moved kibuzzard-69735EB9 24.6 mm to (164.8, 101.3)
- moved kibuzzard-69735EC0 24.6 mm to (184.8, 89.0)
- moved kibuzzard-6846361F 11.8 mm to (183.8, 95.0)
- moved kibuzzard-69799C9D 9.41 mm to (178.8, 87.0), turned to 90 degrees
- moved D101 6.01 mm to (178.8, 91.0)
- moved D901 6.01 mm to (157.8, 91.0)
- moved J101 6.01 mm to (168.3, 91.0)
- moved R101 6.01 mm to (181.8, 91.5)
- moved C901 5.01 mm to (153.9, 93.9), turned to 180 degrees
- moved R901 1.87 mm to (160.3, 93.5), turned to 0 degrees
- turned C902 to 90 degrees
- turned L901 to 90 degrees
- turned L902 to -90 degrees
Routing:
- net SER_CLK: track 181.5 -> 175.0 mm
- net +3V3: track 278.1 -> 284.5 mm
- net SER_DATA: track 26.5 -> 20.5 mm
- net SER_PL: track 178.9 -> 172.9 mm
- net SCL: track 28.3 -> 34.2 mm
- net SDA: track 23.5 -> 29.3 mm
- net GND: track 53.3 -> 55.5 mm, vias 360 -> 361
- net Net-(C902-Pad1): track 13.1 -> 14.1 mm
